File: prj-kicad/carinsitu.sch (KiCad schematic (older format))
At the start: 53 parts, among them P1 BAT, P2 MOT, P3 CONN_3, P4 CONN_1, SW1 SWITCH_SLIDE, U1 ESP8285, U2 MIC2860, U3 MAX17205, U4 SN74LVC1T45, U7 LSM6D3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

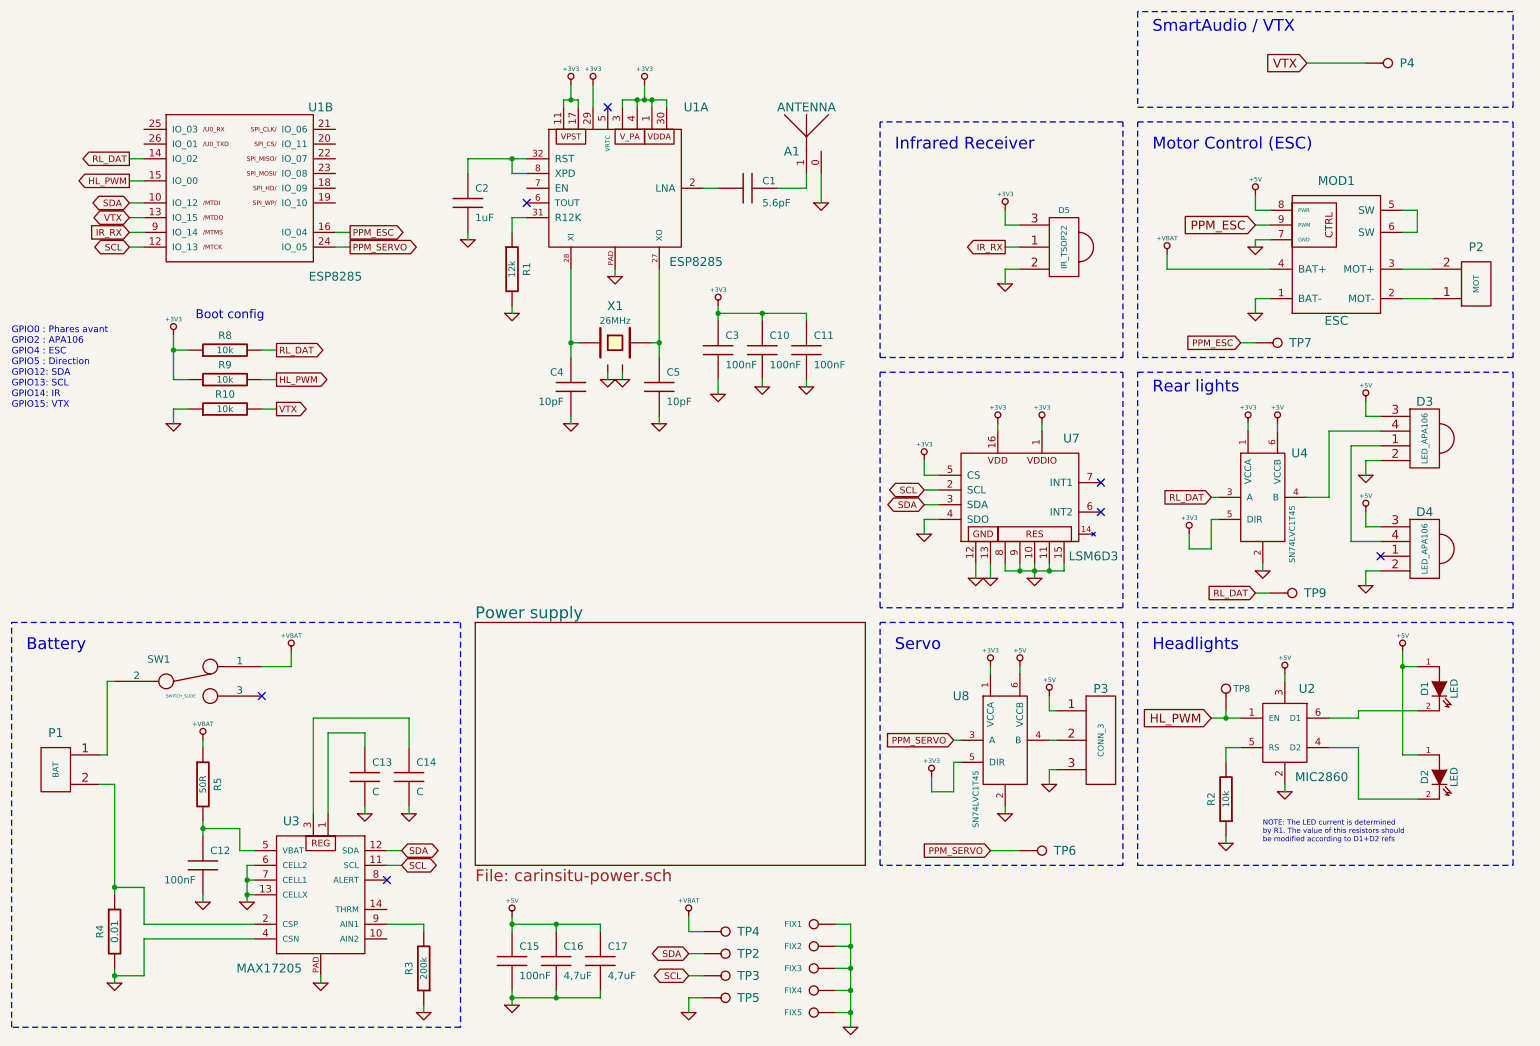
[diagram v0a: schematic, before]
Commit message: = UPD: Improve power, fix 3V3 reg footprint and add routing
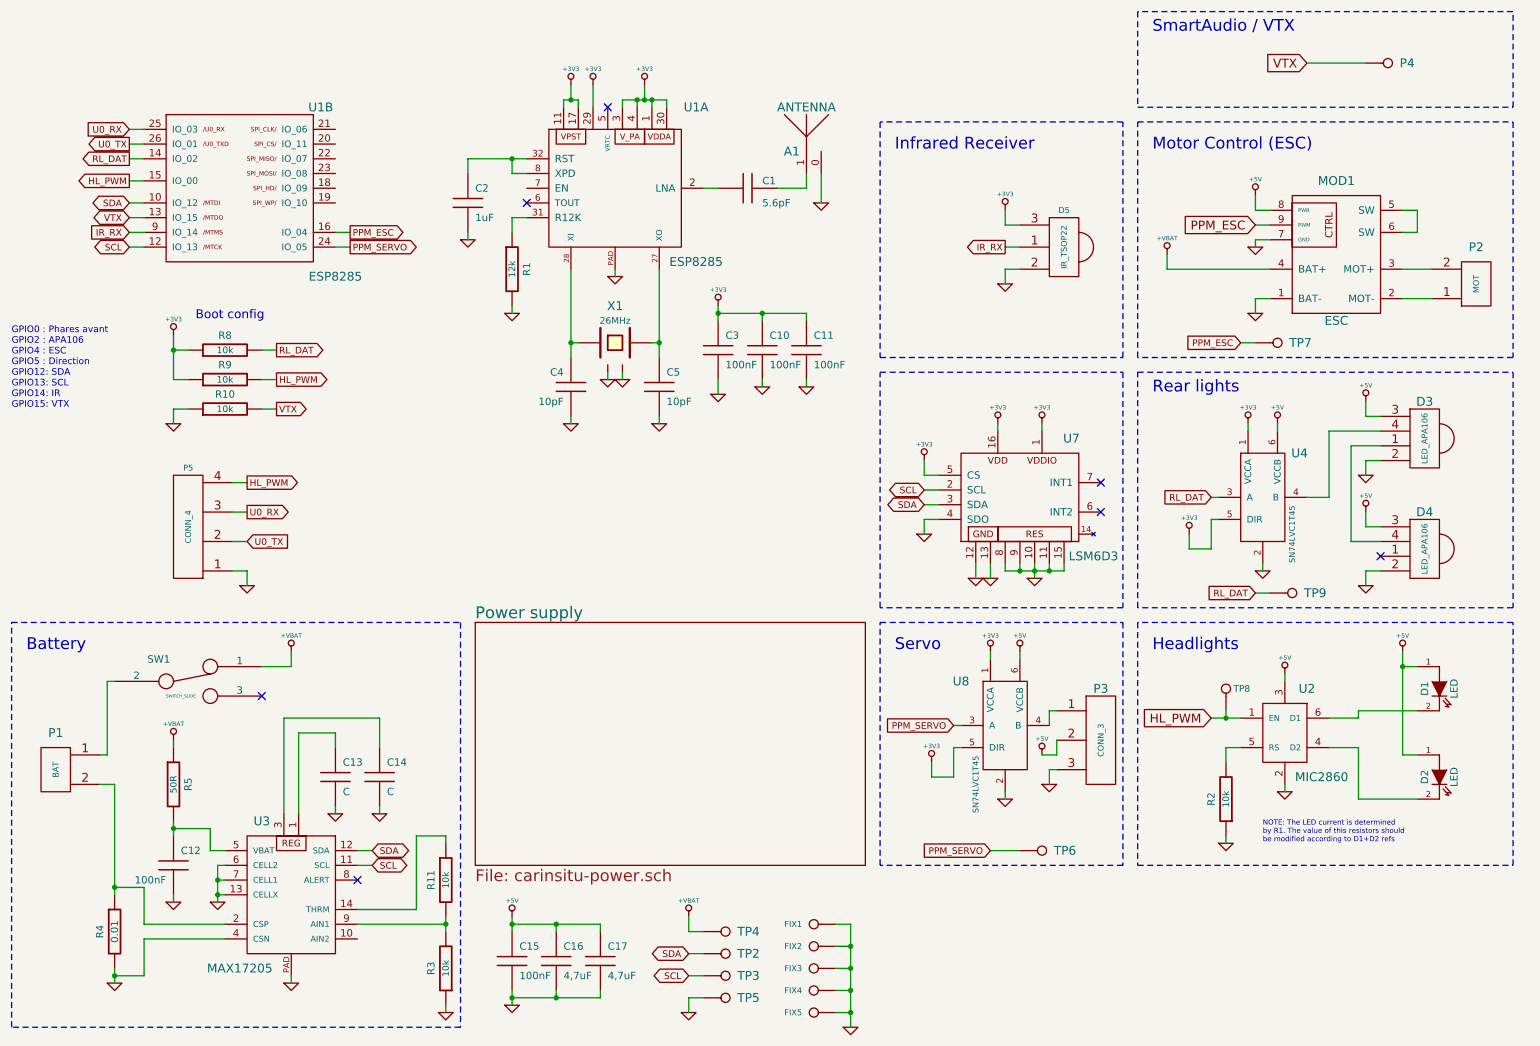
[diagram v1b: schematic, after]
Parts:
- added P5: CONN_4, carinsitu:CONN_61300411121, symbol CONN_4
- added R11: 10k, carinsitu:SMD0603, symbol R
- R3: value 200k -> 10k; footprint carinsitu:SMD0603 -> carinsitu:SMD0805
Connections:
- net +5V: now also P3.2 (P2); no longer P3.1 (P1)
- net GND: now also P5.1 (P1)
- net HL_PWM: now also P5.4
- net at R3.2, U3.9 (AIN1): now also R11.2
- net at U8.4 (B): now also P3.1 (P1); no longer P3.2 (P2)
- net U0_RX: now reaches U1.25 (IO_03)
- net U0_RX: now also P5.3 (P3)
- net U0_TX: now reaches U1.26 (IO_01)
- net U0_TX: now also P5.2 (P2)
- net at U3.14 (THRM): now also R11.1
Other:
- moved on the sheet: C12, C13, C14, R3, R5, U3, U8

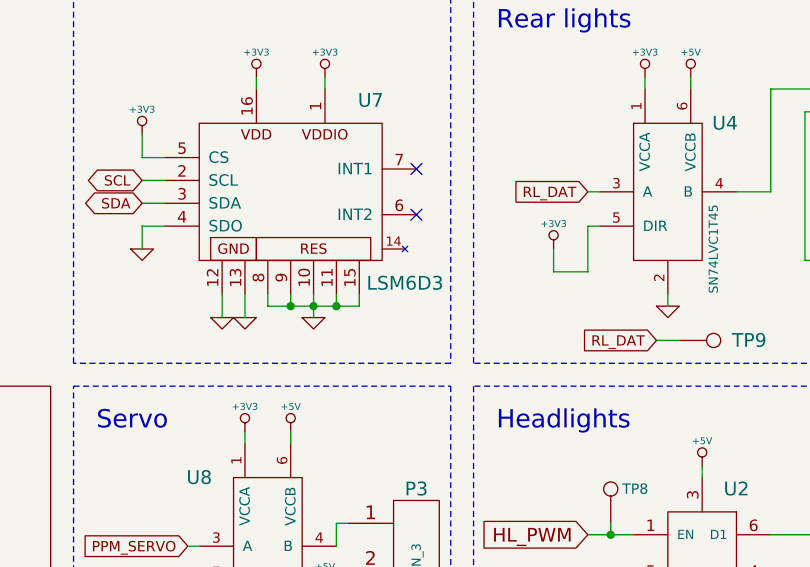
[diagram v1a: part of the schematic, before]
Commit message: = UPD: Add extra-informations on schematics for BOM
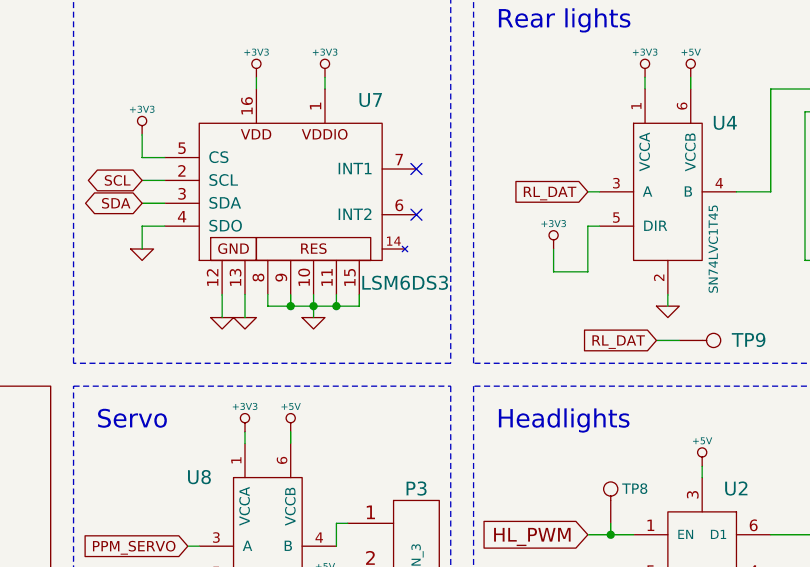
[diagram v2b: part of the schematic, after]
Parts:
- P3: Distrib Ref (none) -> 2356177; Distributor (none) -> Farnell; Manuf Ref (none) -> 61300311021; Manufacturer (none) -> Wurth Elektronik
- R5: Distrib Ref (none) -> 2112878; Distributor (none) -> Farnell; Manuf Ref (none) -> CRCW060350R0FKEA; Manufacturer (none) -> Vishay
- SW1: Distrib Ref (none) -> 2931770; Distributor (none) -> Farnell; Manuf Ref (none) -> L102011ML04Q; Manufacturer (none) -> C&K Components
- U2: Distrib Ref (none) -> 2509995; Distributor (none) -> Farnell; Manuf Ref (none) -> MIC2860-2PYD6; Manufacturer (none) -> Microchip
- U3: Distrib Ref (none) -> 2909787; Distributor (none) -> Farnell; Manuf Ref (none) -> MAX17205G+00E; Manufacturer (none) -> Maxim Integrated
- U7: value LSM6D3 -> LSM6DS3; Distrib Ref (none) -> 2770317; Distributor (none) -> Farnell; Manuf Ref (none) -> LSM6DS3HTR; Manufacturer (none) -> ST
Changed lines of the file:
@@
 F 2 "carinsitu:SOT23-6" H 9550 5500 60  0001 C CNN
 F 3 "" H 9550 5500 60  0000 C CNN
+F 4 "Microchip" H 9550 5500 60  0001 C CNN "Manufacturer"
+F 5 "MIC2860-2PYD6" H 9550 5500 60  0001 C CNN "Manuf Ref"
+F 6 "Farnell" H 9550 5500 60  0001 C CNN "Distributor"
+F 7 "2509995" H 9550 5500 60  0001 C CNN "Distrib Ref"
 	1    9550 5500
 	1    0    0    -1
@@
 F 2 "carinsitu:SW_L102xxxML" H 2100 5150 50  0001 C CNN
 F 3 "" H 2100 5150 50  0000 C CNN
+F 4 "C&K Components" H 2100 5150 60  0001 C CNN "Manufacturer"
+F 5 "L102011ML04Q" H 2100 5150 60  0001 C CNN "Manuf Ref"
+F 6 "Farnell" H 2100 5150 60  0001 C CNN "Distributor"
+F 7 "2931770" H 2100 5150 60  0001 C CNN "Distrib Ref"
 	1    2100 5150
 	1    0    0    -1
@@
 F 2 "carinsitu:SMD0603" H 2000 5850 60  0001 C CNN
 F 3 "" H 2000 5850 60  0000 C CNN
+F 4 "Vishay" V 2000 5850 60  0001 C CNN "Manufacturer"
+F 5 "CRCW060350R0FKEA" V 2000 5850 60  0001 C CNN "Manuf Ref"
+F 6 "Farnell" V 2000 5850 60  0001 C CNN "Distributor"
+F 7 "2112878" V 2000 5850 60  0001 C CNN "Distrib Ref"
 	1    2000 5850
 	1    0    0    -1
@@
 F 2 "carinsitu:CONN_61300311021" H 8300 5550 60  0001 C CNN
 F 3 "" H 8300 5550 60  0000 C CNN
+F 4 "Wurth Elektronik" H 8300 5550 60  0001 C CNN "Manufacturer"
+F 5 "61300311021" H 8300 5550 60  0001 C CNN "Manuf Ref"
+F 6 "Farnell" H 8300 5550 60  0001 C CNN "Distributor"
+F 7 "2356177" H 8300 5550 60  0001 C CNN "Distrib Ref"
 	1    8300 5550
 	1    0    0    -1
@@
 P 7750 3900
 F 0 "U7" H 8100 4300 60  0000 C CNN
-F 1 "LSM6D3" H 8250 3500 60  0000 C CNN
+F 1 "LSM6DS3" H 8250 3500 60  0000 C CNN
 F 2 "carinsitu:LGA-16" H 7750 3900 60  0001 C CNN
 F 3 "" H 7750 3900 60  0000 C CNN
+F 4 "ST" H 7750 3900 60  0001 C CNN "Manufacturer"
+F 5 "LSM6DS3HTR" H 7750 3900 60  0001 C CNN "Manuf Ref"
+F 6 "Farnell" H 7750 3900 60  0001 C CNN "Distributor"
+F 7 "2770317" H 7750 3900 60  0001 C CNN "Distrib Ref"
 	1    7750 3900
 	1    0    0    -1
@@
 F 2 "carinsitu:TDFN14" H 2800 6600 60  0001 C CNN
 F 3 "" H 2800 6600 60  0000 C CNN
+F 4 "Maxim Integrated" H 2800 6600 60  0001 C CNN "Manufacturer"
+F 5 "MAX17205G+00E" H 2800 6600 60  0001 C CNN "Manuf Ref"
+F 6 "Farnell" H 2800 6600 60  0001 C CNN "Distributor"
+F 7 "2909787" H 2800 6600 60  0001 C CNN "Distrib Ref"
 	1    2800 6600
 	-1   0    0    -1

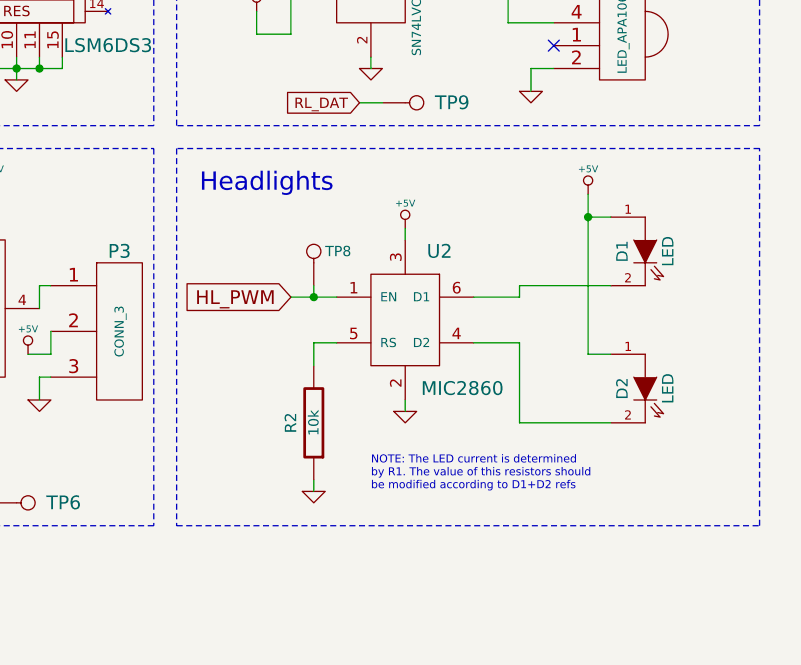
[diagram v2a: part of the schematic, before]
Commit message: = UPD: Move headlights driver and add a logic ic to invert signal
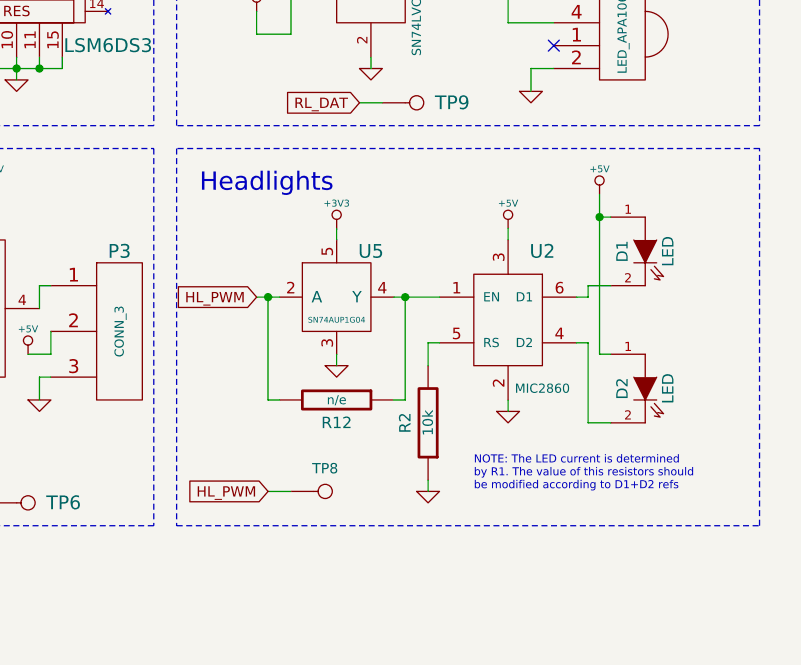
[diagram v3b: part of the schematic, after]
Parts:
- added R12: n/e, carinsitu:SMD0603, symbol R
- added U5: SN74AUP1G04, carinsitu:SC70-5, symbol SN74AUP1G04
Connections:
- net +3V3: now also U5.5
- net GND: now also U5.3
- net HL_PWM: now also R12.2, U5.2 (A); no longer U2.1 (EN)
- new net: R12.1, U2.1 (EN), U5.4 (Y)
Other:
- moved on the sheet: R2, TP8, U2
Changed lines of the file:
@@
 L MIC2860 U2
 U 1 1 5D1330CD
-P 9550 5500
-F 0 "U2" H 9700 5800 60  0000 C CNN
-F 1 "MIC2860" H 9800 5200 60  0000 C CNN
-F 2 "carinsitu:SOT23-6" H 9550 5500 60  0001 C CNN
-F 3 "" H 9550 5500 60  0000 C CNN
-F 4 "Microchip" H 9550 5500 60  0001 C CNN "Manufacturer"
-F 5 "MIC2860-2PYD6" H 9550 5500 60  0001 C CNN "Manuf Ref"
-F 6 "Farnell" H 9550 5500 60  0001 C CNN "Distributor"
-F 7 "2509995" H 9550 5500 60  0001 C CNN "Distrib Ref"
-	1    9550 5500
-	1    0    0    -1
-$EndComp
-Wire Wire Line
-	9850 5400 10050 5400
-Wire Wire Line
-	9850 5600 10050 5600
-Wire Wire Line
-	10050 5600 10050 5950
-Wire Wire Line
-	10050 5950 10450 5950
-Wire Wire Line
-	10050 5400 10050 5350
-Wire Wire Line
-	10050 5350 10450 5350
+P 10000 5500
+F 0 "U2" H 10150 5800 60  0000 C CNN
+F 1 "MIC2860" H 10150 5200 40  0000 C CNN
+F 2 "carinsitu:SOT23-6" H 10000 5500 60  0001 C CNN
+F 3 "" H 10000 5500 60  0000 C CNN
+F 4 "Microchip" H 10000 5500 60  0001 C CNN "Manufacturer"
+F 5 "MIC2860-2PYD6" H 10000 5500 60  0001 C CNN "Manuf Ref"
+F 6 "Farnell" H 10000 5500 60  0001 C CNN "Distributor"
+F 7 "2509995" H 10000 5500 60  0001 C CNN "Distrib Ref"
+	1    10000 5500
+	1    0    0    -1
+$EndComp
 $Comp
 L GND #PWR02
@@
 L +5V #PWR04
 U 1 1 5D133751
-P 10350 4950
-F 0 "#PWR04" H 10350 4910 30  0001 C CNN
-F 1 "+5V" H 10350 5060 30  0000 C CNN
-F 2 "" H 10350 4950 60  0000 C CNN
-F 3 "" H 10350 4950 60  0000 C CNN
-	1    10350 4950
-	1    0    0    -1
-$EndComp
-Wire Wire Line
-	10350 4950 10350 5650
-Wire Wire Line
-	10350 5050 10450 5050
-Wire Wire Line
-	10350 5650 10450 5650
-Connection ~ 10350 5050
+P 10400 4950
+F 0 "#PWR04" H 10400 4910 30  0001 C CNN
+F 1 "+5V" H 10400 5060 30  0000 C CNN
+F 2 "" H 10400 4950 60  0000 C CNN
+F 3 "" H 10400 4950 60  0000 C CNN
+	1    10400 4950
+	1    0    0    -1
+$EndComp
+Wire Wire Line
+	10400 4950 10400 5650
+Connection ~ 10400 5050
 Text Notes 8650 4950 0    80   ~ 0
 Headlights
@@
 L +5V #PWR05
 U 1 1 5D133888
-P 9550 5100
-F 0 "#PWR05" H 9550 5060 30  0001 C CNN
-F 1 "+5V" H 9550 5210 30  0000 C CNN
-F 2 "" H 9550 5100 60  0000 C CNN
-F 3 "" H 9550 5100 60  0000 C CNN
-	1    9550 5100
-	1    0    0    -1
-$EndComp
-Wire Wire Line
-	9550 5100 9550 5150
-Wire Wire Line
-	9550 5900 9550 5850
+P 10000 5100
+F 0 "#PWR05" H 10000 5060 30  0001 C CNN
+F 1 "+5V" H 10000 5210 30  0000 C CNN
+F 2 "" H 10000 5100 60  0000 C CNN
+F 3 "" H 10000 5100 60  0000 C CNN
+	1    10000 5100
+	1    0    0    -1
+$EndComp
+Wire Wire Line
+	10000 5100 10000 5150
+Wire Wire Line
+	10000 5900 10000 5850
 $Comp
 L GND #PWR06
 U 1 1 5D133907
-P 9550 5900
-F 0 "#PWR06" H 9550 5900 30  0001 C CNN
-F 1 "GND" H 9550 5830 30  0001 C CNN
-F 2 "" H 9550 5900 60  0000 C CNN
-F 3 "" H 9550 5900 60  0000 C CNN
-	1    9550 5900
-	1    0    0    -1
-$EndComp
-Text GLabel 9050 5400 0    60   Input ~ 0
+P 10000 5900
+F 0 "#PWR06" H 10000 5900 30  0001 C CNN
+F 1 "GND" H 10000 5830 30  0001 C CNN
+F 2 "" H 10000 5900 60  0000 C CNN
+F 3 "" H 10000 5900 60  0000 C CNN
+	1    10000 5900
+	1    0    0    -1
+$EndComp
+Text GLabel 8900 5400 0    45   Input ~ 0
 HL_PWM
-Wire Wire Line
-	9050 5400 9250 5400
 $Comp
 L R R2
 U 1 1 5D133B4E
-P 9150 5950
-F 0 "R2" V 9250 5950 50  0000 C CNN
-F 1 "10k" V 9150 5950 45  0000 C CNN
-F 2 "carinsitu:SMD0805" H 9150 5950 60  0001 C CNN
-F 3 "" H 9150 5950 60  0000 C CNN
-	1    9150 5950
+P 9650 5950
+F 0 "R2" V 9750 5950 50  0000 C CNN
+F 1 "10k" V 9650 5950 45  0000 C CNN
+F 2 "carinsitu:SMD0805" H 9650 5950 60  0001 C CNN
+F 3 "" H 9650 5950 60  0000 C CNN
+	1    9650 5950
 	-1   0    0    1
 $EndComp
@@
 L GND #PWR07
 U 1 1 5D133C2F
-P 9150 6250
-F 0 "#PWR07" H 9150 6250 30  0001 C CNN
-F 1 "GND" H 9150 6180 30  0001 C CNN
-F 2 "" H 9150 6250 60  0000 C CNN
-F 3 "" H 9150 6250 60  0000 C CNN
-	1    9150 6250
-	1    0    0    -1
-$EndComp
-Wire Wire Line
-	9150 6250 9150 6200
-Wire Wire Line
-	9150 5700 9150 5600
-Wire Wire Line
-	9150 5600 9250 5600
-Text Notes 9400 6250 0    35   ~ 0
+P 9650 6250
+F 0 "#PWR07" H 9650 6250 30  0001 C CNN
+F 1 "GND" H 9650 6180 30  0001 C CNN
+F 2 "" H 9650 6250 60  0000 C CNN
+F 3 "" H 9650 6250 60  0000 C CNN
+	1    9650 6250
+	1    0    0    -1
+$EndComp
+Wire Wire Line
+	9650 6250 9650 6200
+Wire Wire Line
+	9650 5700 9650 5600
+Text Notes 9850 6250 0    35   ~ 0
 NOTE: The LED current is determined\nby R1. The value of this resistors should\nbe modified according to D1+D2 refs
 Text GLabel 3200 2200 2    45   Output ~ 0
@@
 L CONN_1 TP8
 U 1 1 5D2CA28E
-P 9150 5200
-F 0 "TP8" V 9150 5150 45  0000 R CNN
-F 1 "CONN_1" H 9150 5255 30  0001 C CNN
-F 2 "carinsitu:TP" H 9150 5200 60  0001 C CNN
-F 3 "" H 9150 5200 60  0000 C CNN
-	1    9150 5200
-	0    -1   -1   0
-$EndComp
-Wire Wire Line
-	9150 5350 9150 5400
-Connection ~ 9150 5400
+P 9200 6250
+F 0 "TP8" H 9200 6350 45  0000 C CNN
+F 1 "CONN_1" H 9200 6305 30  0001 C CNN
+F 2 "carinsitu:TP" H 9200 6250 60  0001 C CNN
+F 3 "" H 9200 6250 60  0000 C CNN
+	1    9200 6250
+	1    0    0    -1
+$EndComp
 $Comp
 L CONN_1 TP9
@@
 Wire Wire Line
 	7950 5450 7950 5350
+Wire Wire Line
+	10300 5400 10350 5400
+Wire Wire Line
+	10350 5400 10350 5350
+Wire Wire Line
+	10300 5600 10350 5600
+Wire Wire Line
+	10450 5050 10400 5050
+Wire Wire Line
+	10400 5650 10450 5650
+Wire Wire Line
+	10350 5600 10350 5950
+Wire Wire Line
+	10350 5950 10450 5950
+Wire Wire Line
+	10350 5350 10450 5350
+$Comp
+L SN74AUP1G04 U5
+U 1 1 5D6D0FD6
+P 9250 5400
+F 0 "U5" H 9400 5600 60  0000 C CNN
+F 1 "SN74AUP1G04" H 9250 5300 25  0000 C CNN
+F 2 "carinsitu:SC70-5" H 9250 5400 60  0001 C CNN
+F 3 "" H 9250 5400 60  0000 C CNN
+F 4 "Texas Instruments" H 9250 5400 60  0001 C CNN "Manufacturer"
+F 5 "SN74AUP1G04DCKR" H 9250 5400 60  0001 C CNN "Manuf Ref"
+F 6 "Farnell" H 9250 5400 60  0001 C CNN "Distributor"
+F 7 "3006540" H 9250 5400 60  0001 C CNN "Distrib Ref"
+	1    9250 5400
+	1    0    0    -1
+$EndComp
+$Comp
+L +3V3 #PWR064
+U 1 1 5D6D1251
+P 9250 5100
+F 0 "#PWR064" H 9250 5060 30  0001 C CNN
+F 1 "+3V3" H 9250 5210 30  0000 C CNN
+F 2 "" H 9250 5100 60  0000 C CNN
+F 3 "" H 9250 5100 60  0000 C CNN
+	1    9250 5100
+	1    0    0    -1
+$EndComp
+Wire Wire Line
+	9250 5100 9250 5150
+$Comp
+L GND #PWR065
+U 1 1 5D6D145F
+P 9250 5700
+F 0 "#PWR065" H 9250 5700 30  0001 C CNN
+F 1 "GND" H 9250 5630 30  0001 C CNN
+F 2 "" H 9250 5700 60  0000 C CNN
+F 3 "" H 9250 5700 60  0000 C CNN
+	1    9250 5700
+	1    0    0    -1
+$EndComp
+Wire Wire Line
+	9250 5700 9250 5650
+Text GLabel 8950 6250 0    45   Input ~ 0
+HL_PWM
+Wire Wire Line
+	9050 6250 8950 6250
+Wire Wire Line
+	9650 5600 9700 5600
+$Comp
+L R R12
+U 1 1 5D6D2AC5
+P 9250 5850
+F 0 "R12" V 9350 5850 50  0000 C CNN
+F 1 "n/e" V 9250 5850 40  0000 C CNN
+F 2 "carinsitu:SMD0603" H 9250 5850 60  0001 C CNN
+F 3 "" H 9250 5850 60  0000 C CNN
+	1    9250 5850
+	0    1    1    0
+$EndComp
+Wire Wire Line
+	8900 5400 9000 5400
+Wire Wire Line
+	8950 5400 8950 5850
+Wire Wire Line
+	8950 5850 9000 5850
+Connection ~ 8950 5400
+Wire Wire Line
+	9500 5850 9550 5850
+Wire Wire Line
+	9550 5850 9550 5400
+Wire Wire Line
+	9500 5400 9700 5400
+Connection ~ 9550 5400
 $EndSCHEMATC
